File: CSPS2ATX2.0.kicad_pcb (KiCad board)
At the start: 2 copper layers, 67.9 x 87.6 mm, 63 parts, among them J1 Conn_02x32_Counter_Clockwise, J10 IDE/SATA, J101 USB_C_Receptacle_USB2.0, J102 Conn_02x03_Odd_Even, J103 Conn_01x04, J104 Conn_01x04, J2 GW_24p_ATX, J3 GW_PCIe/CPU, J4 GW_PCIe/CPU, J5 GW_PCIe/CPU, J6 GW_PCIe/CPU, J7 GW_PCIe/CPU, J8 GW_PCIe/CPU, J9 IDE/SATA, SW101 SW_Push, U1 TPS3511, U101 ATmega328P-AU, U102 CH340C, U2 PW22ASAB, U3 PW22ASAB, U4 Mini360, Y101 16MHz

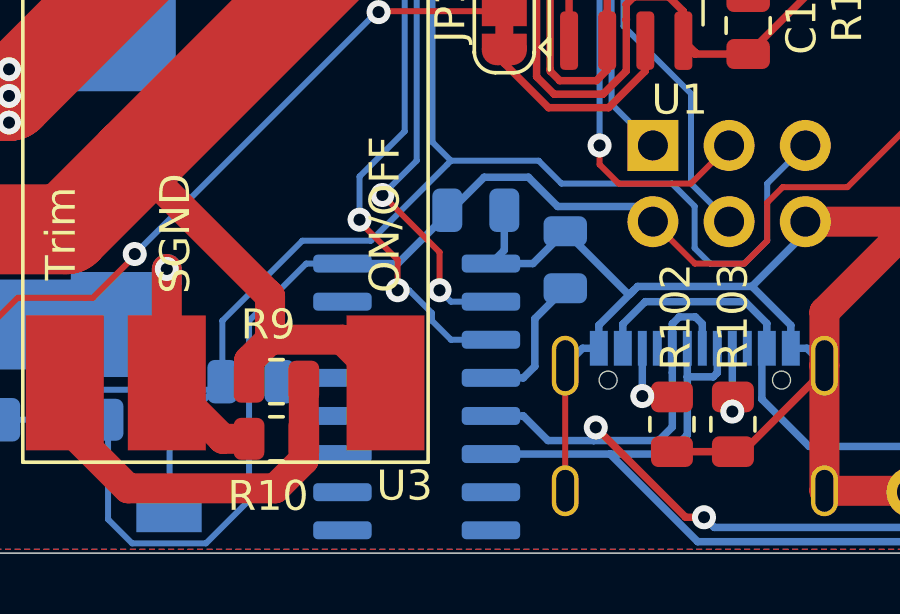
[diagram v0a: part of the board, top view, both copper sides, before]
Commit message: confirm trim resistor
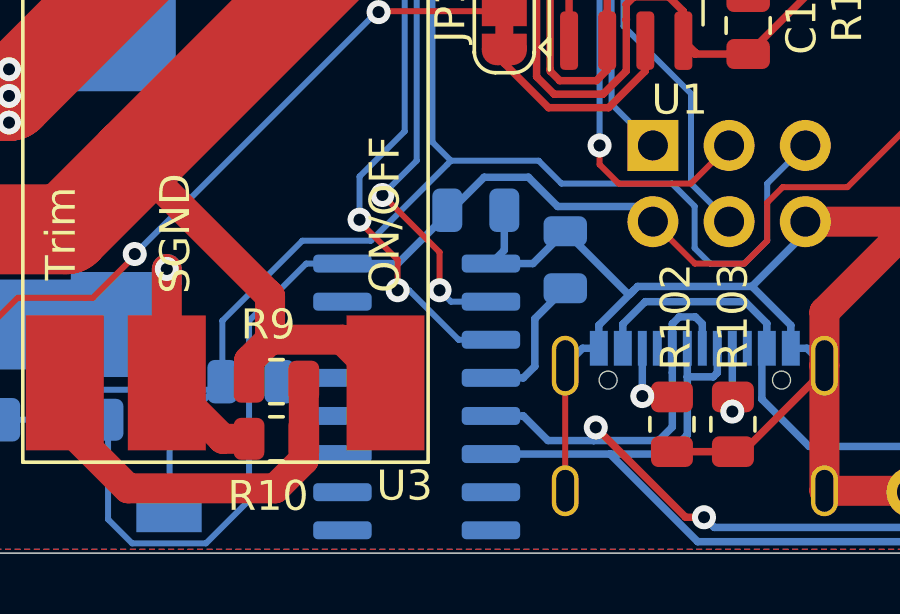
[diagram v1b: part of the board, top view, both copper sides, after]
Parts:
- R10: value R -> 4.4K
- R104: value 30K -> 10K
- R105: value 10K -> 3.3K
- R3: value 22K -> 21K
- R8: value R -> 2.7K
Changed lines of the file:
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@@
     (thickness 1.6)
     (drawings 12)
-    (tracks 913)
+    (tracks 911)
     (zones 0)
     (modules 63)
@@
       (effects (font (size 1 1) (thickness 0.15)))
     )
-    (fp_text value R (at 0 0) (layer F.Fab)
+    (fp_text value 4.4K (at 0 0) (layer F.Fab)
       (effects (font (size 1 1) (thickness 0.15)))
     )
@@
       (effects (font (size 1 1) (thickness 0.15)))
     )
-    (fp_text value R (at 0 0) (layer F.Fab)
+    (fp_text value 2.7K (at 0 0) (layer F.Fab)
       (effects (font (size 1 1) (thickness 0.15)))
     )
@@
       (effects (font (size 1 1) (thickness 0.15)))
     )
-    (fp_text value 10K (at 0 1.65) (layer F.Fab)
+    (fp_text value 3.3K (at 0 1.65) (layer F.Fab)
       (effects (font (size 1 1) (thickness 0.15)))
     )
@@
       (effects (font (size 1 1) (thickness 0.15)))
     )
-    (fp_text value 30K (at 0 1.65) (layer F.Fab)
+    (fp_text value 10K (at 0 1.65) (layer F.Fab)
       (effects (font (size 1 1) (thickness 0.15)))
     )
@@
       (effects (font (size 1 1) (thickness 0.15)))
     )
-    (fp_text value 22K (at 0 1.65 90) (layer F.Fab)
+    (fp_text value 21K (at 0 1.65 90) (layer F.Fab)
       (effects (font (size 1 1) (thickness 0.15)))
     )
@@
   (segment (start 118.402022 90.589022) (end 118.402022 93.256022) (width 0.2) (layer B.Cu) (net 45))
   (segment (start 118.402022 93.256022) (end 126.238 101.092) (width 0.2) (layer B.Cu) (net 45))
-  (segment (start 124.014 117.983) (end 122.682 117.983) (width 0.2) (layer B.Cu) (net 46))
-  (segment (start 122.682 117.983) (end 122.047 117.348) (width 0.2) (layer B.Cu) (net 46))
-  (segment (start 122.047 117.348) (end 122.047 117.094) (width 0.2) (layer B.Cu) (net 46))
-  (segment (start 122.047 117.094) (end 121.285 116.332) (width 0.2) (layer B.Cu) (net 46))
   (via (at 120.904 116.332) (size 0.8) (drill 0.4) (layers F.Cu B.Cu) (net 46))
-  (segment (start 121.285 116.332) (end 120.904 116.332) (width 0.2) (layer B.Cu) (net 46))
   (segment (start 120.904 116.332) (end 120.904 115.316) (width 0.2) (layer F.Cu) (net 46))
   (segment (start 120.904 115.316) (end 119.634 114.046) (width 0.2) (layer F.Cu) (net 46))
@@
   (segment (start 110.242077 96.907077) (end 100.203 86.868) (width 0.2) (layer B.Cu) (net 46))
   (segment (start 117.989074 96.907077) (end 110.242077 96.907077) (width 0.2) (layer B.Cu) (net 46))
+  (segment (start 122.936 117.983) (end 121.285 116.332) (width 0.2) (layer B.Cu) (net 46))
+  (segment (start 121.285 116.332) (end 120.904 116.332) (width 0.2) (layer B.Cu) (net 46))
+  (segment (start 124.014 117.983) (end 122.936 117.983) (width 0.2) (layer B.Cu) (net 46))
   (segment (start 124.014 116.713) (end 122.682 116.713) (width 0.2) (layer B.Cu) (net 47))
   (via (at 122.301 116.332) (size 0.8) (drill 0.4) (layers F.Cu B.Cu) (net 47))

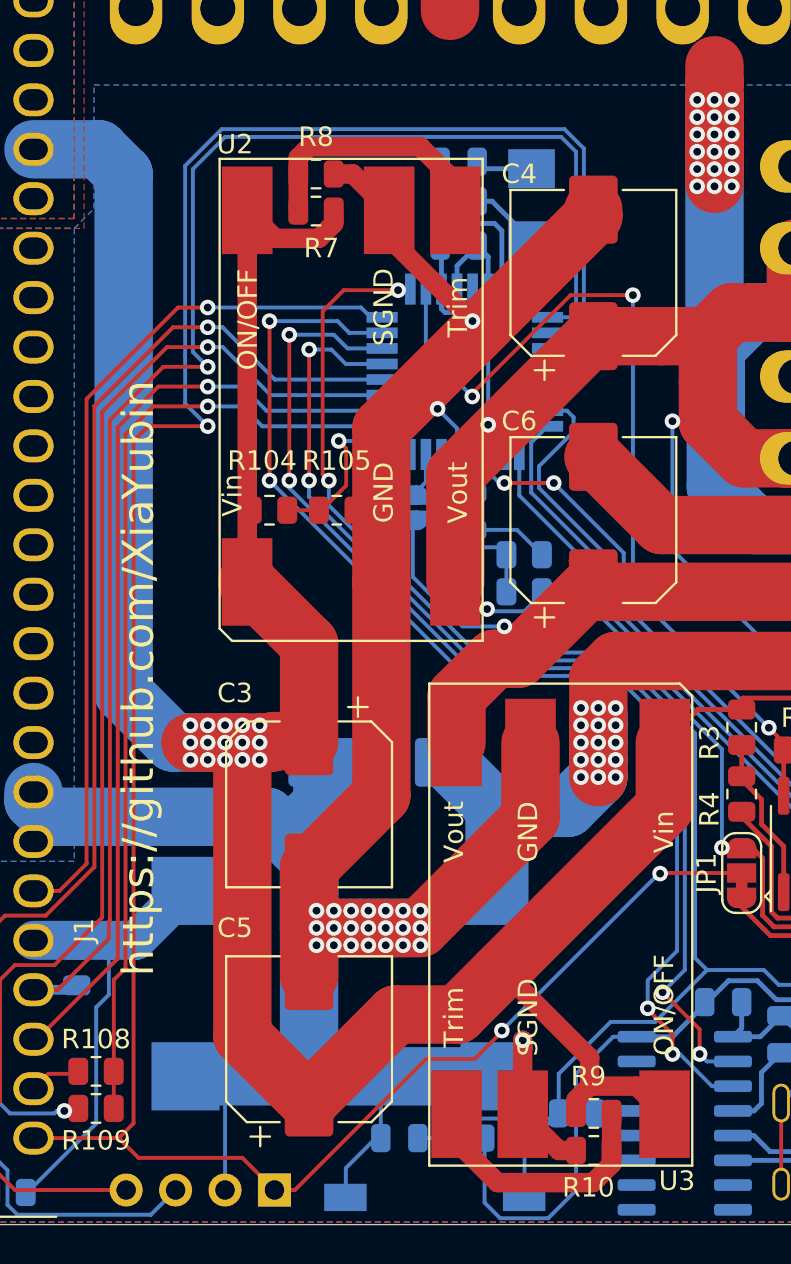
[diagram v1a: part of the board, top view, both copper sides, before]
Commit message: remove R7 R9
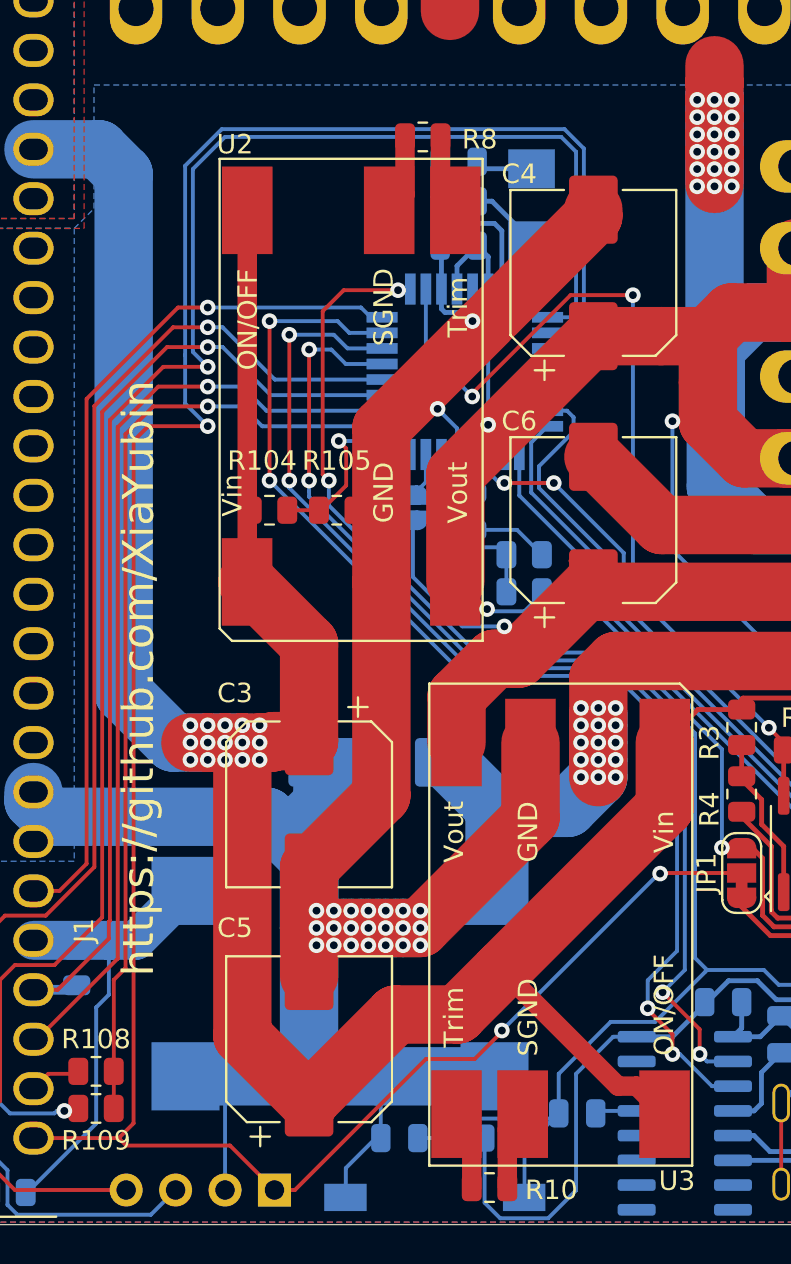
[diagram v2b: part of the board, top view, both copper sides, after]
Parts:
- removed R7, R9: R, Resistor_SMD:R_0805_2012Metric
- moved R8 5.81 mm to (108.1, 69.2), turned to 0 degrees
- moved R10 5.69 mm to (111.5, 123.2)
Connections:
- R10 pad 1: GND -> Net-(R10-Pad1)
- R8 pad 1: GND -> Net-(R8-Pad1)
- U2 pad 5: GND -> Net-(R8-Pad1)
- U3 pad 4: Net-(R10-Pad2) -> Net-(R10-Pad1)
- U3 pad 5: GND -> Net-(R10-Pad2)
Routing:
- net GND: track 460.8 -> 438.3 mm, vias 43 -> 42
- net Net-(R10-Pad2): track 13.2 -> 4.10 mm
- net +12V: track 255.3 -> 246.8 mm
- net Net-(R8-Pad2): track 13.3 -> 5.55 mm
- net Net-(R8-Pad1): track 0.00 -> 7.13 mm
- net Net-(R10-Pad1): track 0.00 -> 5.50 mm
